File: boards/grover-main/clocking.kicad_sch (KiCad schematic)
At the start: 30 parts

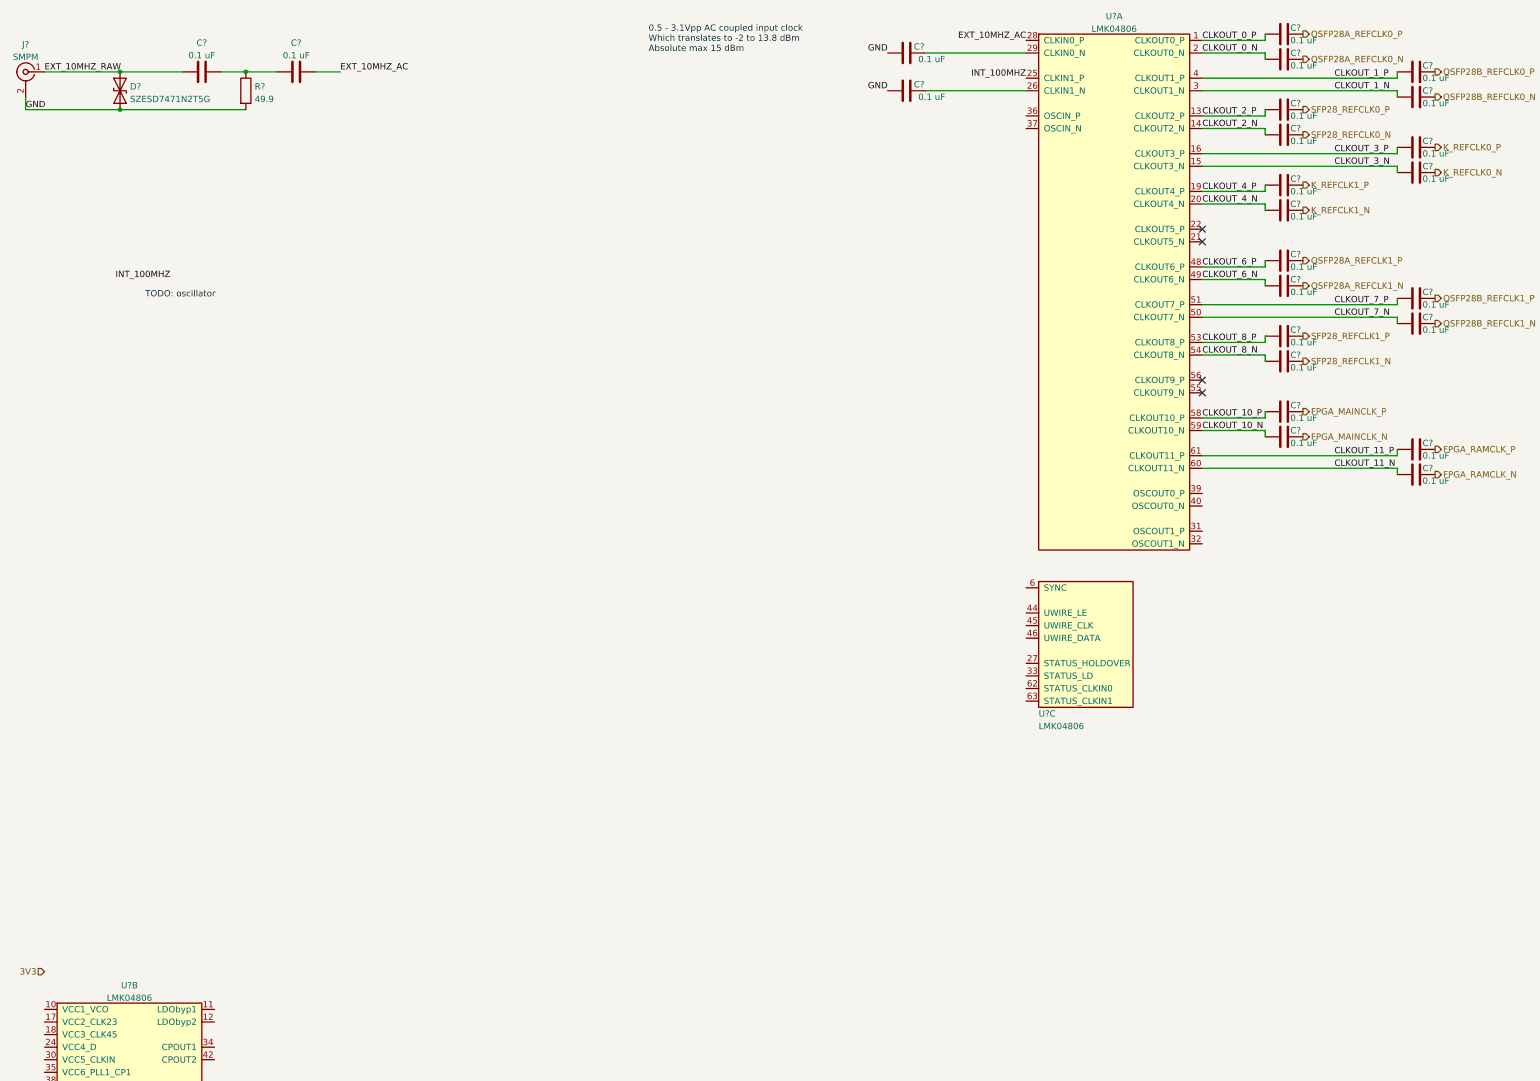
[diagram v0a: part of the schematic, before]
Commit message: Continued initial schematic capture
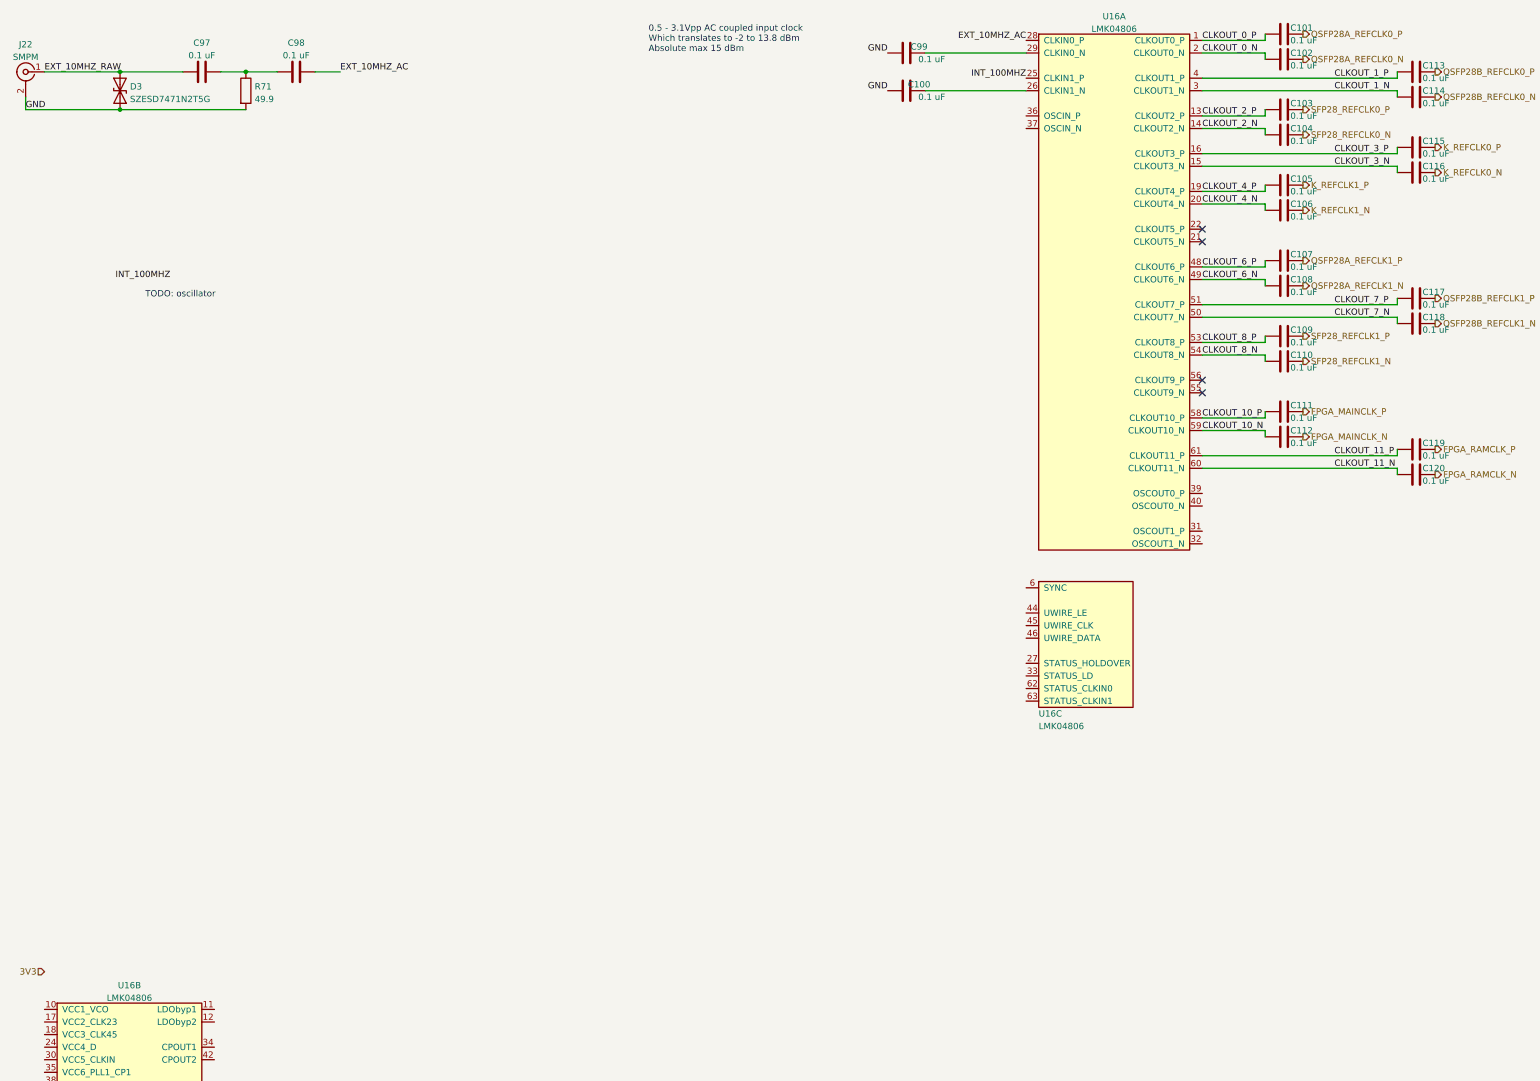
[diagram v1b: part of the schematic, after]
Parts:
- gave numbers to parts that had none: 28
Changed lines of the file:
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@@
   (symbol (lib_id "device:C") (at 279.4 106.68 90) (unit 1)
     (in_bom yes) (on_board yes)
-    (property "Reference" "C?" (id 0) (at 280.67 105.41 90)
+    (property "Reference" "C112" (id 0) (at 280.67 105.41 90)
       (effects (font (size 1.27 1.27)) (justify right))
     )
@@
   (symbol (lib_id "device:C") (at 279.4 101.6 90) (unit 1)
     (in_bom yes) (on_board yes)
-    (property "Reference" "C?" (id 0) (at 280.67 100.33 90)
+    (property "Reference" "C111" (id 0) (at 280.67 100.33 90)
       (effects (font (size 1.27 1.27)) (justify right))
     )
@@
   (symbol (lib_id "conn:CONN_COAXIAL") (at 25.4 33.02 0) (mirror y) (unit 1)
     (in_bom yes) (on_board yes) (fields_autoplaced)
-    (property "Reference" "J?" (id 0) (at 25.3999 27.4936 0))
+    (property "Reference" "J22" (id 0) (at 25.3999 27.4936 0))
     (property "Value" "SMPM" (id 1) (at 25.3999 30.0305 0))
     (property "Footprint" "" (id 2) (at 25.4 33.02 0)
@@
   (symbol (lib_id "device:C") (at 60.96 33.02 90) (unit 1)
     (in_bom yes) (on_board yes) (fields_autoplaced)
-    (property "Reference" "C?" (id 0) (at 60.96 27.1612 90))
+    (property "Reference" "C97" (id 0) (at 60.96 27.1612 90))
     (property "Value" "0.1 uF" (id 1) (at 60.96 29.6981 90))
     (property "Footprint" "" (id 2) (at 64.77 32.0548 0)
@@
   (symbol (lib_id "device:C") (at 279.4 76.2 90) (unit 1)
     (in_bom yes) (on_board yes)
-    (property "Reference" "C?" (id 0) (at 280.67 74.93 90)
+    (property "Reference" "C108" (id 0) (at 280.67 74.93 90)
       (effects (font (size 1.27 1.27)) (justify right))
     )
@@
   (symbol (lib_id "device:C") (at 306.07 78.74 90) (unit 1)
     (in_bom yes) (on_board yes)
-    (property "Reference" "C?" (id 0) (at 307.34 77.47 90)
+    (property "Reference" "C117" (id 0) (at 307.34 77.47 90)
       (effects (font (size 1.27 1.27)) (justify right))
     )
@@
   (symbol (lib_id "special-azonenberg:LMK04806") (at 31.75 261.62 0) (unit 2)
     (in_bom yes) (on_board yes) (fields_autoplaced)
-    (property "Reference" "U?" (id 0) (at 46.355 217.4072 0))
+    (property "Reference" "U16" (id 0) (at 46.355 217.4072 0))
     (property "Value" "LMK04806" (id 1) (at 46.355 219.9441 0))
     (property "Footprint" "" (id 2) (at 31.75 261.62 0)
@@
   (symbol (lib_id "device:C") (at 306.07 114.3 90) (unit 1)
     (in_bom yes) (on_board yes)
-    (property "Reference" "C?" (id 0) (at 307.34 113.03 90)
+    (property "Reference" "C120" (id 0) (at 307.34 113.03 90)
       (effects (font (size 1.27 1.27)) (justify right))
     )
@@
   (symbol (lib_id "device:C") (at 306.07 109.22 90) (unit 1)
     (in_bom yes) (on_board yes)
-    (property "Reference" "C?" (id 0) (at 307.34 107.95 90)
+    (property "Reference" "C119" (id 0) (at 307.34 107.95 90)
       (effects (font (size 1.27 1.27)) (justify right))
     )
@@
   (symbol (lib_id "device:C") (at 306.07 33.02 90) (unit 1)
     (in_bom yes) (on_board yes)
-    (property "Reference" "C?" (id 0) (at 307.34 31.75 90)
+    (property "Reference" "C113" (id 0) (at 307.34 31.75 90)
       (effects (font (size 1.27 1.27)) (justify right))
     )
@@
   (symbol (lib_id "device:C") (at 279.4 60.96 90) (unit 1)
     (in_bom yes) (on_board yes)
-    (property "Reference" "C?" (id 0) (at 280.67 59.69 90)
+    (property "Reference" "C106" (id 0) (at 280.67 59.69 90)
       (effects (font (size 1.27 1.27)) (justify right))
     )
@@
   (symbol (lib_id "device:C") (at 279.4 55.88 90) (unit 1)
     (in_bom yes) (on_board yes)
-    (property "Reference" "C?" (id 0) (at 280.67 54.61 90)
+    (property "Reference" "C105" (id 0) (at 280.67 54.61 90)
       (effects (font (size 1.27 1.27)) (justify right))
     )
@@
   (symbol (lib_id "device:C") (at 80.01 33.02 90) (unit 1)
     (in_bom yes) (on_board yes) (fields_autoplaced)
-    (property "Reference" "C?" (id 0) (at 80.01 27.1612 90))
+    (property "Reference" "C98" (id 0) (at 80.01 27.1612 90))
     (property "Value" "0.1 uF" (id 1) (at 80.01 29.6981 90))
     (property "Footprint" "" (id 2) (at 83.82 32.0548 0)
@@
   (symbol (lib_id "device:C") (at 306.07 48.26 90) (unit 1)
     (in_bom yes) (on_board yes)
-    (property "Reference" "C?" (id 0) (at 307.34 46.99 90)
+    (property "Reference" "C115" (id 0) (at 307.34 46.99 90)
       (effects (font (size 1.27 1.27)) (justify right))
     )
@@
   (symbol (lib_id "device:C") (at 279.4 45.72 90) (unit 1)
     (in_bom yes) (on_board yes)
-    (property "Reference" "C?" (id 0) (at 280.67 44.45 90)
+    (property "Reference" "C104" (id 0) (at 280.67 44.45 90)
       (effects (font (size 1.27 1.27)) (justify right))
     )
@@
   (symbol (lib_id "device:C") (at 279.4 71.12 90) (unit 1)
     (in_bom yes) (on_board yes)
-    (property "Reference" "C?" (id 0) (at 280.67 69.85 90)
+    (property "Reference" "C107" (id 0) (at 280.67 69.85 90)
       (effects (font (size 1.27 1.27)) (justify right))
     )
@@
   (symbol (lib_id "device:C") (at 306.07 38.1 90) (unit 1)
     (in_bom yes) (on_board yes)
-    (property "Reference" "C?" (id 0) (at 307.34 36.83 90)
+    (property "Reference" "C114" (id 0) (at 307.34 36.83 90)
       (effects (font (size 1.27 1.27)) (justify right))
     )
@@
   (symbol (lib_id "device:C") (at 279.4 40.64 90) (unit 1)
     (in_bom yes) (on_board yes)
-    (property "Reference" "C?" (id 0) (at 280.67 39.37 90)
+    (property "Reference" "C103" (id 0) (at 280.67 39.37 90)
       (effects (font (size 1.27 1.27)) (justify right))
     )
@@
   (symbol (lib_id "device:C") (at 279.4 86.36 90) (unit 1)
     (in_bom yes) (on_board yes)
-    (property "Reference" "C?" (id 0) (at 280.67 85.09 90)
+    (property "Reference" "C109" (id 0) (at 280.67 85.09 90)
       (effects (font (size 1.27 1.27)) (justify right))
     )
@@
   (symbol (lib_id "device:C") (at 279.4 30.48 90) (unit 1)
     (in_bom yes) (on_board yes)
-    (property "Reference" "C?" (id 0) (at 280.67 29.21 90)
+    (property "Reference" "C102" (id 0) (at 280.67 29.21 90)
       (effects (font (size 1.27 1.27)) (justify right))
     )
@@
   (symbol (lib_id "special-azonenberg:LMK04806") (at 229.87 161.29 0) (unit 3)
     (in_bom yes) (on_board yes)
-    (property "Reference" "U?" (id 0) (at 229.87 162.56 0)
+    (property "Reference" "U16" (id 0) (at 229.87 162.56 0)
       (effects (font (size 1.27 1.27)) (justify left))
     )
@@
   (symbol (lib_id "device:R") (at 69.85 36.83 0) (unit 1)
     (in_bom yes) (on_board yes) (fields_autoplaced)
-    (property "Reference" "R?" (id 0) (at 71.628 35.9953 0)
+    (property "Reference" "R71" (id 0) (at 71.628 35.9953 0)
       (effects (font (size 1.27 1.27)) (justify left))
     )
@@
   (symbol (lib_id "device:C") (at 279.4 25.4 90) (unit 1)
     (in_bom yes) (on_board yes)
-    (property "Reference" "C?" (id 0) (at 280.67 24.13 90)
+    (property "Reference" "C101" (id 0) (at 280.67 24.13 90)
       (effects (font (size 1.27 1.27)) (justify right))
     )
@@
   (symbol (lib_id "device:C") (at 279.4 91.44 90) (unit 1)
     (in_bom yes) (on_board yes)
-    (property "Reference" "C?" (id 0) (at 280.67 90.17 90)
+    (property "Reference" "C110" (id 0) (at 280.67 90.17 90)
       (effects (font (size 1.27 1.27)) (justify right))
     )
@@
   (symbol (lib_id "device:C") (at 203.2 29.21 90) (unit 1)
     (in_bom yes) (on_board yes)
-    (property "Reference" "C?" (id 0) (at 205.74 27.94 90))
+    (property "Reference" "C99" (id 0) (at 205.74 27.94 90))
     (property "Value" "0.1 uF" (id 1) (at 208.28 30.48 90))
     (property "Footprint" "" (id 2) (at 207.01 28.2448 0)
@@
   (symbol (lib_id "device:C") (at 203.2 36.83 90) (unit 1)
     (in_bom yes) (on_board yes)
-    (property "Reference" "C?" (id 0) (at 205.74 35.56 90))
+    (property "Reference" "C100" (id 0) (at 205.74 35.56 90))
     (property "Value" "0.1 uF" (id 1) (at 208.28 38.1 90))
     (property "Footprint" "" (id 2) (at 207.01 35.8648 0)
@@
   (symbol (lib_id "device:C") (at 306.07 83.82 90) (unit 1)
     (in_bom yes) (on_board yes)
-    (property "Reference" "C?" (id 0) (at 307.34 82.55 90)
+    (property "Reference" "C118" (id 0) (at 307.34 82.55 90)
       (effects (font (size 1.27 1.27)) (justify right))
     )
@@
   (symbol (lib_id "device:D_TVS") (at 44.45 36.83 90) (unit 1)
     (in_bom yes) (on_board yes) (fields_autoplaced)
-    (property "Reference" "D?" (id 0) (at 46.4566 35.9953 90)
+    (property "Reference" "D3" (id 0) (at 46.4566 35.9953 90)
       (effects (font (size 1.27 1.27)) (justify right))
     )
@@
   (symbol (lib_id "device:C") (at 306.07 53.34 90) (unit 1)
     (in_bom yes) (on_board yes)
-    (property "Reference" "C?" (id 0) (at 307.34 52.07 90)
+    (property "Reference" "C116" (id 0) (at 307.34 52.07 90)
       (effects (font (size 1.27 1.27)) (justify right))
     )
@@
   (symbol (lib_id "special-azonenberg:LMK04806") (at 229.87 129.54 0) (unit 1)
     (in_bom yes) (on_board yes) (fields_autoplaced)
-    (property "Reference" "U?" (id 0) (at 245.11 21.8272 0))
+    (property "Reference" "U16" (id 0) (at 245.11 21.8272 0))
     (property "Value" "LMK04806" (id 1) (at 245.11 24.3641 0))
     (property "Footprint" "" (id 2) (at 229.87 129.54 0)
